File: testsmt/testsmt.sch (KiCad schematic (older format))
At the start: 29 parts

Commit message: schematic nearly done
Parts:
- removed R?: R, symbol Device:R
- added D? (x7): LED, symbol Device:LED
- added R? (x8): 68, symbol Device:R
- R?: value R -> 68
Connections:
- net +3V3: now also U?.10 (~SRCLR), U?.16 (3.3V), U?.16 (VCC), U?.16 (VDD), U?.50 (3.3V)
- net FSR: now also U?.4 (X7)
- net GND: now also D?.1 (K), U?.1 (GND), U?.13 (~OE), U?.17 (GND), U?.39 (GND), U?.8 (GND), D?.1 (K), D?.1 (K), D?.1 (K), D?.1 (K), D?.1 (K), D?.1 (K), D?.1 (K)
- net KNOB_2: now also U?.14 (X1)
- net KNOB_3: now also U?.15 (X2)
- net KNOB_4: now also U?.12 (X3)
- net KNOB_5: now also U?.1 (X4)
- net KNOB_6: now also U?.5 (X5)
- net KNOB_READ: now also U?.3 (X)
- net LDR: now also U?.2 (X6)
- net SHIFT_REG_CLOCK: now also U?.11 (SRCLK)
- net SHIFT_REG_DATA: now also U?.14 (SER)
- net SHIFT_REG_LATCH: now also U?.12 (RCLK)
- net at D?.2 (A): now also R?.1
- net at R?.2: now also U?.1 (QB)
- net at U?.15 (QA): now also R?.2
- net at U?.2 (QC): now also R?.2
- net at U?.3 (QD): now also R?.2
- net at U?.4 (QE): now also R?.2
- net at U?.5 (QF): now also R?.2
- net at U?.6 (QG): now also R?.2
- net at U?.7 (QH): now also R?.2
- new net: D?.2 (A), R?.1 (x7)
- no-connect marks 8 -> 33
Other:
- moved on the sheet: D?, J?, R?, U?

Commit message: schematic looking good
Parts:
- removed U? (x2): 4051, symbol 4xxx:4051
- added C1: C, symbol Device:C
- added C2: 10uF, symbol Device:CP
- added J5: AudioJack3_Ground_Switch, symbol Connector:AudioJack3_Ground_Switch
- added R2: 220, symbol Device:R
- added R3: 470, symbol Device:R
- added RV7: R_POT, symbol Device:R_POT
- gave numbers to parts that had none: 41
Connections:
- net SINGLE_LED is gone; now on an unnamed net: U2.21 (14_A0_SCK)
- net +3V3: now also R3.2; no longer U2.50 (3.3V)
- net DAC_OUTPUT: now also RV7.3
- net GND: now also D1.1 (K), C1.2, J5.S, RV7.1
- net SERIAL_RX: now also U1.6 (VO2), R3.1
- net at D1.2 (A): now also R1.1
- net at J1.4: now also R2.2
- net at J1.5: now also D2.2 (A), U1.3 (C2)
- net +5V: now reaches U2.33 (Vin)
- net +5V: now also U1.8 (VCC), C1.1
- net at U1.2 (C1): now also D2.1 (K), R2.1
- new net: C2.2, J5.R, J5.T
- new net: C2.1, RV7.2
- no-connect marks 33 -> 39
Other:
- moved on the sheet: D1, D2, J1, R1, R4, R5, R6, R7, RV1, RV2, RV3, RV4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

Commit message: nearly done adding footprints
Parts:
- C1: value C -> 0.1uF; footprint (none) -> Capacitor_SMD:C_0805_2012Metric
- C2: footprint (none) -> Capacitor_Tantalum_SMD:CP_EIA-3216-18_Kemet-A
- D1, D10, D3, D4, D5, D6, D7, D8, D9: footprint (none) -> LED_SMD:LED_0805_2012Metric
- D2: footprint Diode_THT:D_DO-35_SOD27_P7.62mm_Horizontal -> Diode_SMD:D_SOD-123
- J2, J3, J4: footprint (none) -> Connector_PinSocket_2.54mm:PinSocket_1x16_P2.54mm_Vertical
- R1, R10, R11, R12, R13, R14, R15, R2, R3, R5, R7, R8, R9: footprint (none) -> Resistor_SMD:R_0805_2012Metric
- R4, R6: footprint (none) -> Connector_PinHeader_2.54mm:PinHeader_1x02_P2.54mm_Vertical
- U1: footprint (none) -> Package_DIP:SMDIP-8_W9.53mm
- U2: footprint (none) -> teensy:Teensy30_31_32_LC
- U3, U4, U5, U6, U7, U8: footprint (none) -> Package_SO:SOIC-16_3.9x9.9mm_P1.27mm
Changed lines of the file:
@@
 F 0 "U4" H 7291 9746 50  0000 L CNN
 F 1 "4051" H 7291 9655 50  0000 L CNN
-F 2 "" H 6750 9700 50  0001 C CNN
+F 2 "Package_SO:SOIC-16_3.9x9.9mm_P1.27mm" H 6750 9700 50  0001 C CNN
 F 3 "http://www.intersil.com/content/dam/Intersil/documents/cd40/cd4051bms-52bms-53bms.pdf" H 6750 9700 50  0001 C CNN
 	1    6750 9700
@@
 F 0 "U7" H 11241 4446 50  0000 L CNN
 F 1 "4051" H 11241 4355 50  0000 L CNN
-F 2 "" H 10700 4400 50  0001 C CNN
+F 2 "Package_SO:SOIC-16_3.9x9.9mm_P1.27mm" H 10700 4400 50  0001 C CNN
 F 3 "http://www.intersil.com/content/dam/Intersil/documents/cd40/cd4051bms-52bms-53bms.pdf" H 10700 4400 50  0001 C CNN
 	1    10700 4400
@@
 F 0 "D1" H 941 7416 50  0000 C CNN
 F 1 "LED" H 941 7325 50  0000 C CNN
-F 2 "" H 950 7200 50  0001 C CNN
+F 2 "LED_SMD:LED_0805_2012Metric" H 950 7200 50  0001 C CNN
 F 3 "~" H 950 7200 50  0001 C CNN
 	1    950  7200
@@
 F 0 "D4" H 13941 1816 50  0000 C CNN
 F 1 "LED" H 13941 1725 50  0000 C CNN
-F 2 "" H 13950 1600 50  0001 C CNN
+F 2 "LED_SMD:LED_0805_2012Metric" H 13950 1600 50  0001 C CNN
 F 3 "~" H 13950 1600 50  0001 C CNN
 	1    13950 1600
@@
 F 0 "R9" H 13720 1646 50  0000 L CNN
 F 1 "68" H 13720 1555 50  0000 L CNN
-F 2 "" V 13580 1600 50  0001 C CNN
+F 2 "Resistor_SMD:R_0805_2012Metric" V 13580 1600 50  0001 C CNN
 F 3 "~" H 13650 1600 50  0001 C CNN
 	1    13650 1600
@@
 F 0 "U2" H 3200 7587 60  0000 C CNN
 F 1 "Teensy3.2" H 3200 7481 60  0000 C CNN
-F 2 "" H 3200 5200 60  0000 C CNN
+F 2 "teensy:Teensy30_31_32_LC" H 3200 5200 60  0001 C CNN
 F 3 "" H 3200 5200 60  0000 C CNN
 	1    3200 6000
@@
 F 0 "J2" H 11880 7092 50  0000 L CNN
 F 1 "Conn_01x16" H 11880 7001 50  0000 L CNN
-F 2 "" H 11800 7100 50  0001 C CNN
+F 2 "Connector_PinSocket_2.54mm:PinSocket_1x16_P2.54mm_Vertical" H 11800 7100 50  0001 C CNN
 F 3 "~" H 11800 7100 50  0001 C CNN
 	1    11800 7100
@@
 F 0 "U1" H 3000 2967 50  0000 C CNN
 F 1 "6N138" H 3000 2876 50  0000 C CNN
-F 2 "" H 3290 2200 50  0001 C CNN
+F 2 "Package_DIP:SMDIP-8_W9.53mm" H 3290 2200 50  0001 C CNN
 F 3 "http://www.onsemi.com/pub/Collateral/HCPL2731-D.pdf" H 3290 2200 50  0001 C CNN
 	1    3000 2500
@@
 F 0 "D2" H 2350 2566 50  0000 C CNN
 F 1 "1N4148" H 2350 2475 50  0000 C CNN
-F 2 "Diode_THT:D_DO-35_SOD27_P7.62mm_Horizontal" H 2350 2175 50  0001 C CNN
+F 2 "Diode_SMD:D_SOD-123" H 2350 2175 50  0001 C CNN
 F 3 "http://www.nxp.com/documents/data_sheet/1N4148_1N4448.pdf" H 2350 2350 50  0001 C CNN
 	1    2350 2350
@@
 F 0 "U3" H 7291 7246 50  0000 L CNN
 F 1 "4051" H 7291 7155 50  0000 L CNN
-F 2 "" H 6750 7200 50  0001 C CNN
+F 2 "Package_SO:SOIC-16_3.9x9.9mm_P1.27mm" H 6750 7200 50  0001 C CNN
 F 3 "http://www.intersil.com/content/dam/Intersil/documents/cd40/cd4051bms-52bms-53bms.pdf" H 6750 7200 50  0001 C CNN
 	1    6750 7200
@@
 F 0 "U8" H 11550 1250 50  0000 C CNN
 F 1 "74HC595" H 11550 1150 50  0000 C CNN
-F 2 "" H 12200 1600 50  0001 C CNN
+F 2 "Package_SO:SOIC-16_3.9x9.9mm_P1.27mm" H 12200 1600 50  0001 C CNN
 F 3 "http://www.ti.com/lit/ds/symlink/sn74hc595.pdf" H 12200 1600 50  0001 C CNN
 	1    12200 1600
@@
 F 0 "U6" H 9991 9746 50  0000 L CNN
 F 1 "4051" H 9991 9655 50  0000 L CNN
-F 2 "" H 9450 9700 50  0001 C CNN
+F 2 "Package_SO:SOIC-16_3.9x9.9mm_P1.27mm" H 9450 9700 50  0001 C CNN
 F 3 "http://www.intersil.com/content/dam/Intersil/documents/cd40/cd4051bms-52bms-53bms.pdf" H 9450 9700 50  0001 C CNN
 	1    9450 9700
@@
 F 0 "U5" H 9991 7246 50  0000 L CNN
 F 1 "4051" H 9991 7155 50  0000 L CNN
-F 2 "" H 9450 7200 50  0001 C CNN
+F 2 "Package_SO:SOIC-16_3.9x9.9mm_P1.27mm" H 9450 7200 50  0001 C CNN
 F 3 "http://www.intersil.com/content/dam/Intersil/documents/cd40/cd4051bms-52bms-53bms.pdf" H 9450 7200 50  0001 C CNN
 	1    9450 7200
@@
 F 0 "J3" H 13180 7092 50  0000 L CNN
 F 1 "Conn_01x16" H 13180 7001 50  0000 L CNN
-F 2 "" H 13100 7100 50  0001 C CNN
+F 2 "Connector_PinSocket_2.54mm:PinSocket_1x16_P2.54mm_Vertical" H 13100 7100 50  0001 C CNN
 F 3 "~" H 13100 7100 50  0001 C CNN
 	1    13100 7100
@@
 F 0 "J4" H 14480 7092 50  0000 L CNN
 F 1 "Conn_01x16" H 14480 7001 50  0000 L CNN
-F 2 "" H 14400 7100 50  0001 C CNN
+F 2 "Connector_PinSocket_2.54mm:PinSocket_1x16_P2.54mm_Vertical" H 14400 7100 50  0001 C CNN
 F 3 "~" H 14400 7100 50  0001 C CNN
 	1    14400 7100
@@
 F 0 "R6" H 6920 4996 50  0000 L CNN
 F 1 "R_FORCE" H 6920 4905 50  0000 L CNN
-F 2 "" V 6900 4700 50  0001 L CNN
+F 2 "Connector_PinHeader_2.54mm:PinHeader_1x02_P2.54mm_Vertical" V 6900 4700 50  0001 L CNN
 F 3 "~" H 6850 4900 50  0001 C CNN
 	1    6850 4950
@@
 F 0 "R4" H 6120 4996 50  0000 L CNN
 F 1 "R_PHOTO" H 6120 4905 50  0000 L CNN
-F 2 "" V 6100 4700 50  0001 L CNN
+F 2 "Connector_PinHeader_2.54mm:PinHeader_1x02_P2.54mm_Vertical" V 6100 4700 50  0001 L CNN
 F 3 "~" H 6050 4900 50  0001 C CNN
 	1    6050 4950
@@
 F 0 "R5" H 6120 5496 50  0000 L CNN
 F 1 "10K" H 6120 5405 50  0000 L CNN
-F 2 "" V 5980 5450 50  0001 C CNN
+F 2 "Resistor_SMD:R_0805_2012Metric" V 5980 5450 50  0001 C CNN
 F 3 "~" H 6050 5450 50  0001 C CNN
 	1    6050 5450
@@
 F 0 "R7" H 6920 5496 50  0000 L CNN
 F 1 "10K" H 6920 5405 50  0000 L CNN
-F 2 "" V 6780 5450 50  0001 C CNN
+F 2 "Resistor_SMD:R_0805_2012Metric" V 6780 5450 50  0001 C CNN
 F 3 "~" H 6850 5450 50  0001 C CNN
 	1    6850 5450
@@
 F 0 "D3" H 13941 1416 50  0000 C CNN
 F 1 "LED" H 13941 1325 50  0000 C CNN
-F 2 "" H 13950 1200 50  0001 C CNN
+F 2 "LED_SMD:LED_0805_2012Metric" H 13950 1200 50  0001 C CNN
 F 3 "~" H 13950 1200 50  0001 C CNN
 	1    13950 1200
@@
 F 0 "R8" H 13720 1246 50  0000 L CNN
 F 1 "68" H 13720 1155 50  0000 L CNN
-F 2 "" V 13580 1200 50  0001 C CNN
+F 2 "Resistor_SMD:R_0805_2012Metric" V 13580 1200 50  0001 C CNN
 F 3 "~" H 13650 1200 50  0001 C CNN
 	1    13650 1200
@@
 F 0 "D6" H 13941 2616 50  0000 C CNN
 F 1 "LED" H 13941 2525 50  0000 C CNN
-F 2 "" H 13950 2400 50  0001 C CNN
+F 2 "LED_SMD:LED_0805_2012Metric" H 13950 2400 50  0001 C CNN
 F 3 "~" H 13950 2400 50  0001 C CNN
 	1    13950 2400
@@
 F 0 "R11" H 13720 2446 50  0000 L CNN
 F 1 "68" H 13720 2355 50  0000 L CNN
-F 2 "" V 13580 2400 50  0001 C CNN
+F 2 "Resistor_SMD:R_0805_2012Metric" V 13580 2400 50  0001 C CNN
 F 3 "~" H 13650 2400 50  0001 C CNN
 	1    13650 2400
@@
 F 0 "D5" H 13941 2216 50  0000 C CNN
 F 1 "LED" H 13941 2125 50  0000 C CNN
-F 2 "" H 13950 2000 50  0001 C CNN
+F 2 "LED_SMD:LED_0805_2012Metric" H 13950 2000 50  0001 C CNN
 F 3 "~" H 13950 2000 50  0001 C CNN
 	1    13950 2000
@@
 F 0 "R10" H 13720 2046 50  0000 L CNN
 F 1 "68" H 13720 1955 50  0000 L CNN
-F 2 "" V 13580 2000 50  0001 C CNN
+F 2 "Resistor_SMD:R_0805_2012Metric" V 13580 2000 50  0001 C CNN
 F 3 "~" H 13650 2000 50  0001 C CNN
 	1    13650 2000
@@
 F 0 "D8" H 13941 3416 50  0000 C CNN
 F 1 "LED" H 13941 3325 50  0000 C CNN
-F 2 "" H 13950 3200 50  0001 C CNN
+F 2 "LED_SMD:LED_0805_2012Metric" H 13950 3200 50  0001 C CNN
 F 3 "~" H 13950 3200 50  0001 C CNN
 	1    13950 3200
@@
 F 0 "R13" H 13720 3246 50  0000 L CNN
 F 1 "68" H 13720 3155 50  0000 L CNN
-F 2 "" V 13580 3200 50  0001 C CNN
+F 2 "Resistor_SMD:R_0805_2012Metric" V 13580 3200 50  0001 C CNN
 F 3 "~" H 13650 3200 50  0001 C CNN
 	1    13650 3200
@@
 F 0 "D7" H 13941 3016 50  0000 C CNN
 F 1 "LED" H 13941 2925 50  0000 C CNN
-F 2 "" H 13950 2800 50  0001 C CNN
+F 2 "LED_SMD:LED_0805_2012Metric" H 13950 2800 50  0001 C CNN
 F 3 "~" H 13950 2800 50  0001 C CNN
 	1    13950 2800
@@
 F 0 "R12" H 13720 2846 50  0000 L CNN
 F 1 "68" H 13720 2755 50  0000 L CNN
-F 2 "" V 13580 2800 50  0001 C CNN
+F 2 "Resistor_SMD:R_0805_2012Metric" V 13580 2800 50  0001 C CNN
 F 3 "~" H 13650 2800 50  0001 C CNN
 	1    13650 2800
@@
 F 0 "D10" H 13941 4216 50  0000 C CNN
 F 1 "LED" H 13941 4125 50  0000 C CNN
-F 2 "" H 13950 4000 50  0001 C CNN
+F 2 "LED_SMD:LED_0805_2012Metric" H 13950 4000 50  0001 C CNN
 F 3 "~" H 13950 4000 50  0001 C CNN
 	1    13950 4000
@@
 F 0 "R15" H 13720 4046 50  0000 L CNN
 F 1 "68" H 13720 3955 50  0000 L CNN
-F 2 "" V 13580 4000 50  0001 C CNN
+F 2 "Resistor_SMD:R_0805_2012Metric" V 13580 4000 50  0001 C CNN
 F 3 "~" H 13650 4000 50  0001 C CNN
 	1    13650 4000
@@
 F 0 "D9" H 13941 3816 50  0000 C CNN
 F 1 "LED" H 13941 3725 50  0000 C CNN
-F 2 "" H 13950 3600 50  0001 C CNN
+F 2 "LED_SMD:LED_0805_2012Metric" H 13950 3600 50  0001 C CNN
 F 3 "~" H 13950 3600 50  0001 C CNN
 	1    13950 3600
@@
 F 0 "R14" H 13720 3646 50  0000 L CNN
 F 1 "68" H 13720 3555 50  0000 L CNN
-F 2 "" V 13580 3600 50  0001 C CNN
+F 2 "Resistor_SMD:R_0805_2012Metric" V 13580 3600 50  0001 C CNN
 F 3 "~" H 13650 3600 50  0001 C CNN
 	1    13650 3600
@@
 F 0 "R1" H 1020 6946 50  0000 L CNN
 F 1 "68" H 1020 6855 50  0000 L CNN
-F 2 "" V 880 6900 50  0001 C CNN
+F 2 "Resistor_SMD:R_0805_2012Metric" V 880 6900 50  0001 C CNN
 F 3 "~" H 950 6900 50  0001 C CNN
 	1    950  6900
@@
 F 0 "R2" V 1843 2000 50  0000 C CNN
 F 1 "220" V 1934 2000 50  0000 C CNN
-F 2 "" V 1980 2000 50  0001 C CNN
+F 2 "Resistor_SMD:R_0805_2012Metric" V 1980 2000 50  0001 C CNN
 F 3 "~" H 2050 2000 50  0001 C CNN
 	1    2050 2000
@@
 F 0 "R3" H 3430 1904 50  0000 R CNN
 F 1 "470" H 3430 1995 50  0000 R CNN
-F 2 "" V 3430 1950 50  0001 C CNN
+F 2 "Resistor_SMD:R_0805_2012Metric" V 3430 1950 50  0001 C CNN
 F 3 "~" H 3500 1950 50  0001 C CNN
 	1    3500 1950
@@
 P 5000 2550
 F 0 "C1" H 5115 2596 50  0000 L CNN
-F 1 "C" H 5115 2505 50  0000 L CNN
-F 2 "" H 5038 2400 50  0001 C CNN
+F 1 "0.1uF" H 5115 2505 50  0000 L CNN
+F 2 "Capacitor_SMD:C_0805_2012Metric" H 5038 2400 50  0001 C CNN
 F 3 "~" H 5000 2550 50  0001 C CNN
 	1    5000 2550
@@
 F 0 "C2" V 7645 2300 50  0000 C CNN
 F 1 "10uF" V 7736 2300 50  0000 C CNN
-F 2 "" H 7938 2150 50  0001 C CNN
+F 2 "Capacitor_Tantalum_SMD:CP_EIA-3216-18_Kemet-A" H 7938 2150 50  0001 C CNN
 F 3 "~" H 7900 2300 50  0001 C CNN
 	1    7900 2300

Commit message: footprints hopefully done
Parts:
- J1: footprint (none) -> polymodsmt:MIDI_DIN5
- J5: footprint (none) -> polymodsmt:Tayda_3.5mm_stereo_TRS_jack_A-853
- RV1, RV2, RV3, RV4, RV5, RV6, RV7: footprint (none) -> Potentiometer_THT:Potentiometer_Alps_RK09K_Single_Vertical
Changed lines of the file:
@@
 F 0 "RV1" H 5980 3796 50  0000 R CNN
 F 1 "R_POT" H 5980 3705 50  0000 R CNN
-F 2 "" H 6050 3750 50  0001 C CNN
+F 2 "Potentiometer_THT:Potentiometer_Alps_RK09K_Single_Vertical" H 6050 3750 50  0001 C CNN
 F 3 "~" H 6050 3750 50  0001 C CNN
 	1    6050 3750
@@
 F 0 "J1" H 1700 2226 50  0000 C CNN
 F 1 "DIN-5_180degree" H 1700 2135 50  0000 C CNN
-F 2 "" H 1700 2500 50  0001 C CNN
+F 2 "polymodsmt:MIDI_DIN5" H 1700 2500 50  0001 C CNN
 F 3 "http://www.mouser.com/ds/2/18/40_c091_abd_e-75918.pdf" H 1700 2500 50  0001 C CNN
 	1    1700 2500
@@
 F 0 "RV3" H 6780 3796 50  0000 R CNN
 F 1 "R_POT" H 6780 3705 50  0000 R CNN
-F 2 "" H 6850 3750 50  0001 C CNN
+F 2 "Potentiometer_THT:Potentiometer_Alps_RK09K_Single_Vertical" H 6850 3750 50  0001 C CNN
 F 3 "~" H 6850 3750 50  0001 C CNN
 	1    6850 3750
@@
 F 0 "RV5" H 7580 3796 50  0000 R CNN
 F 1 "R_POT" H 7580 3705 50  0000 R CNN
-F 2 "" H 7650 3750 50  0001 C CNN
+F 2 "Potentiometer_THT:Potentiometer_Alps_RK09K_Single_Vertical" H 7650 3750 50  0001 C CNN
 F 3 "~" H 7650 3750 50  0001 C CNN
 	1    7650 3750
@@
 F 0 "RV2" H 5980 4396 50  0000 R CNN
 F 1 "R_POT" H 5980 4305 50  0000 R CNN
-F 2 "" H 6050 4350 50  0001 C CNN
+F 2 "Potentiometer_THT:Potentiometer_Alps_RK09K_Single_Vertical" H 6050 4350 50  0001 C CNN
 F 3 "~" H 6050 4350 50  0001 C CNN
 	1    6050 4350
@@
 F 0 "RV4" H 6780 4396 50  0000 R CNN
 F 1 "R_POT" H 6780 4305 50  0000 R CNN
-F 2 "" H 6850 4350 50  0001 C CNN
+F 2 "Potentiometer_THT:Potentiometer_Alps_RK09K_Single_Vertical" H 6850 4350 50  0001 C CNN
 F 3 "~" H 6850 4350 50  0001 C CNN
 	1    6850 4350
@@
 F 0 "RV6" H 7580 4396 50  0000 R CNN
 F 1 "R_POT" H 7580 4305 50  0000 R CNN
-F 2 "" H 7650 4350 50  0001 C CNN
+F 2 "Potentiometer_THT:Potentiometer_Alps_RK09K_Single_Vertical" H 7650 4350 50  0001 C CNN
 F 3 "~" H 7650 4350 50  0001 C CNN
 	1    7650 4350
@@
 F 0 "J5" H 7254 2442 50  0000 C CNN
 F 1 "AudioJack3_Ground_Switch" H 7254 2351 50  0000 C CNN
-F 2 "" H 7250 2100 50  0001 C CNN
+F 2 "polymodsmt:Tayda_3.5mm_stereo_TRS_jack_A-853" H 7250 2100 50  0001 C CNN
 F 3 "~" H 7250 2100 50  0001 C CNN
 	1    7250 2100
@@
 F 0 "RV7" H 8280 2346 50  0000 R CNN
 F 1 "R_POT" H 8280 2255 50  0000 R CNN
-F 2 "" H 8350 2300 50  0001 C CNN
+F 2 "Potentiometer_THT:Potentiometer_Alps_RK09K_Single_Vertical" H 8350 2300 50  0001 C CNN
 F 3 "~" H 8350 2300 50  0001 C CNN
 	1    8350 2300

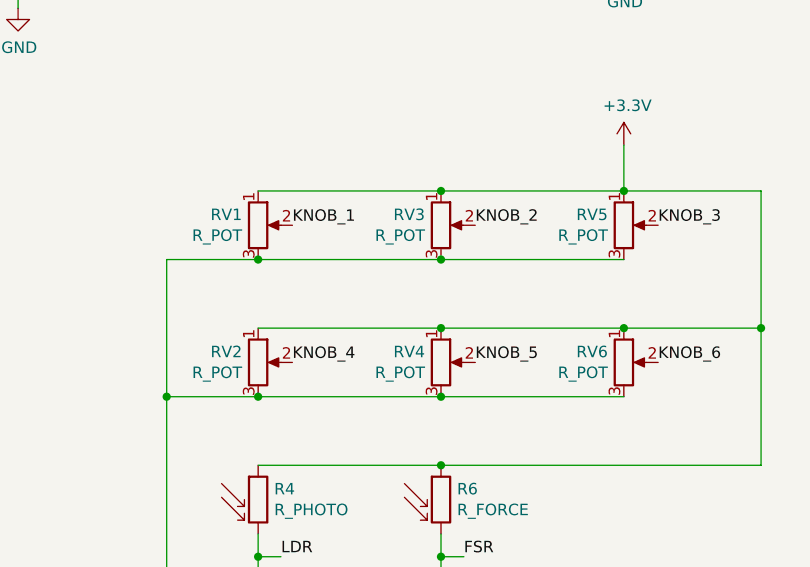
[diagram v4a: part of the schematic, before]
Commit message: started laying out board
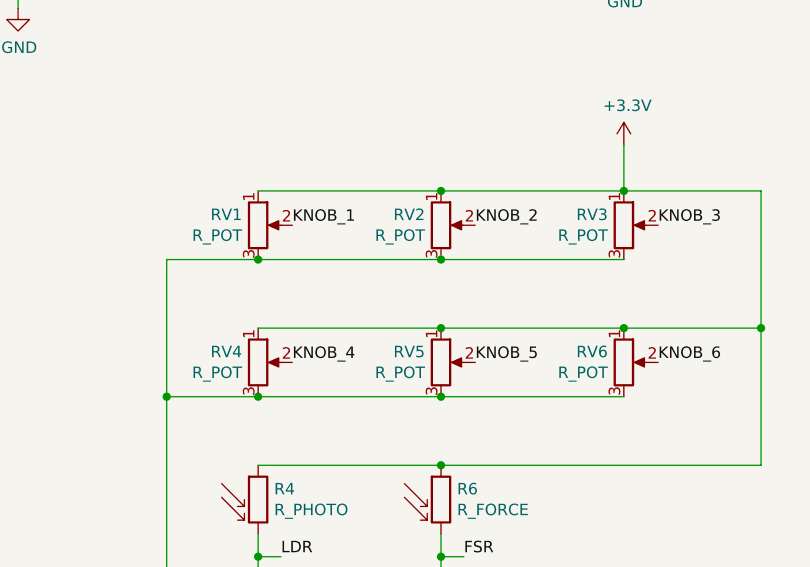
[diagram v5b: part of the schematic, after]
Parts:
- renumbered RV3 to RV2, RV5 to RV3, RV2 to RV4, RV4 to RV5
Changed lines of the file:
@@
 KNOB_1
 $Comp
-L Device:R_POT RV3
+L Device:R_POT RV2
 U 1 1 5E828549
 P 6850 3750
-F 0 "RV3" H 6780 3796 50  0000 R CNN
+F 0 "RV2" H 6780 3796 50  0000 R CNN
 F 1 "R_POT" H 6780 3705 50  0000 R CNN
 F 2 "Potentiometer_THT:Potentiometer_Alps_RK09K_Single_Vertical" H 6850 3750 50  0001 C CNN
@@
 KNOB_2
 $Comp
-L Device:R_POT RV5
+L Device:R_POT RV3
 U 1 1 5E828A25
 P 7650 3750
-F 0 "RV5" H 7580 3796 50  0000 R CNN
+F 0 "RV3" H 7580 3796 50  0000 R CNN
 F 1 "R_POT" H 7580 3705 50  0000 R CNN
 F 2 "Potentiometer_THT:Potentiometer_Alps_RK09K_Single_Vertical" H 7650 3750 50  0001 C CNN
@@
 KNOB_3
 $Comp
-L Device:R_POT RV2
+L Device:R_POT RV4
 U 1 1 5E828A2D
 P 6050 4350
-F 0 "RV2" H 5980 4396 50  0000 R CNN
+F 0 "RV4" H 5980 4396 50  0000 R CNN
 F 1 "R_POT" H 5980 4305 50  0000 R CNN
 F 2 "Potentiometer_THT:Potentiometer_Alps_RK09K_Single_Vertical" H 6050 4350 50  0001 C CNN
@@
 KNOB_4
 $Comp
-L Device:R_POT RV4
+L Device:R_POT RV5
 U 1 1 5E82949C
 P 6850 4350
-F 0 "RV4" H 6780 4396 50  0000 R CNN
+F 0 "RV5" H 6780 4396 50  0000 R CNN
 F 1 "R_POT" H 6780 4305 50  0000 R CNN
 F 2 "Potentiometer_THT:Potentiometer_Alps_RK09K_Single_Vertical" H 6850 4350 50  0001 C CNN

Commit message: mounting holes
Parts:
- added H1, H2, H3, H4: MountingHole, polymodsmt:MountingHole_3.2mm_M3, symbol Mechanical:MountingHole
- RV1, RV2, RV3, RV4, RV5, RV6, RV7: footprint Potentiometer_THT:Potentiometer_Alps_RK09K_Single_Vertical -> polymodsmt:Potentiometer_Alps_RK09K_Single_Vertical
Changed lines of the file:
@@
 F 0 "RV1" H 5980 3796 50  0000 R CNN
 F 1 "R_POT" H 5980 3705 50  0000 R CNN
-F 2 "Potentiometer_THT:Potentiometer_Alps_RK09K_Single_Vertical" H 6050 3750 50  0001 C CNN
+F 2 "polymodsmt:Potentiometer_Alps_RK09K_Single_Vertical" H 6050 3750 50  0001 C CNN
 F 3 "~" H 6050 3750 50  0001 C CNN
 	1    6050 3750
@@
 F 0 "RV2" H 6780 3796 50  0000 R CNN
 F 1 "R_POT" H 6780 3705 50  0000 R CNN
-F 2 "Potentiometer_THT:Potentiometer_Alps_RK09K_Single_Vertical" H 6850 3750 50  0001 C CNN
+F 2 "polymodsmt:Potentiometer_Alps_RK09K_Single_Vertical" H 6850 3750 50  0001 C CNN
 F 3 "~" H 6850 3750 50  0001 C CNN
 	1    6850 3750
@@
 F 0 "RV3" H 7580 3796 50  0000 R CNN
 F 1 "R_POT" H 7580 3705 50  0000 R CNN
-F 2 "Potentiometer_THT:Potentiometer_Alps_RK09K_Single_Vertical" H 7650 3750 50  0001 C CNN
+F 2 "polymodsmt:Potentiometer_Alps_RK09K_Single_Vertical" H 7650 3750 50  0001 C CNN
 F 3 "~" H 7650 3750 50  0001 C CNN
 	1    7650 3750
@@
 F 0 "RV4" H 5980 4396 50  0000 R CNN
 F 1 "R_POT" H 5980 4305 50  0000 R CNN
-F 2 "Potentiometer_THT:Potentiometer_Alps_RK09K_Single_Vertical" H 6050 4350 50  0001 C CNN
+F 2 "polymodsmt:Potentiometer_Alps_RK09K_Single_Vertical" H 6050 4350 50  0001 C CNN
 F 3 "~" H 6050 4350 50  0001 C CNN
 	1    6050 4350
@@
 F 0 "RV5" H 6780 4396 50  0000 R CNN
 F 1 "R_POT" H 6780 4305 50  0000 R CNN
-F 2 "Potentiometer_THT:Potentiometer_Alps_RK09K_Single_Vertical" H 6850 4350 50  0001 C CNN
+F 2 "polymodsmt:Potentiometer_Alps_RK09K_Single_Vertical" H 6850 4350 50  0001 C CNN
 F 3 "~" H 6850 4350 50  0001 C CNN
 	1    6850 4350
@@
 F 0 "RV6" H 7580 4396 50  0000 R CNN
 F 1 "R_POT" H 7580 4305 50  0000 R CNN
-F 2 "Potentiometer_THT:Potentiometer_Alps_RK09K_Single_Vertical" H 7650 4350 50  0001 C CNN
+F 2 "polymodsmt:Potentiometer_Alps_RK09K_Single_Vertical" H 7650 4350 50  0001 C CNN
 F 3 "~" H 7650 4350 50  0001 C CNN
 	1    7650 4350
@@
 F 0 "RV7" H 8280 2346 50  0000 R CNN
 F 1 "R_POT" H 8280 2255 50  0000 R CNN
-F 2 "Potentiometer_THT:Potentiometer_Alps_RK09K_Single_Vertical" H 8350 2300 50  0001 C CNN
+F 2 "polymodsmt:Potentiometer_Alps_RK09K_Single_Vertical" H 8350 2300 50  0001 C CNN
 F 3 "~" H 8350 2300 50  0001 C CNN
 	1    8350 2300
@@
 	7550 2300 7750 2300
 Connection ~ 7550 2300
+$Comp
+L Mechanical:MountingHole H1
+U 1 1 5E851B11
+P 1750 9100
+F 0 "H1" H 1850 9146 50  0000 L CNN
+F 1 "MountingHole" H 1850 9055 50  0000 L CNN
+F 2 "polymodsmt:MountingHole_3.2mm_M3" H 1750 9100 50  0001 C CNN
+F 3 "~" H 1750 9100 50  0001 C CNN
+	1    1750 9100
+	1    0    0    -1
+$EndComp
+$Comp
+L Mechanical:MountingHole H2
+U 1 1 5E851CE3
+P 1750 9350
+F 0 "H2" H 1850 9396 50  0000 L CNN
+F 1 "MountingHole" H 1850 9305 50  0000 L CNN
+F 2 "polymodsmt:MountingHole_3.2mm_M3" H 1750 9350 50  0001 C CNN
+F 3 "~" H 1750 9350 50  0001 C CNN
+	1    1750 9350
+	1    0    0    -1
+$EndComp
+$Comp
+L Mechanical:MountingHole H3
+U 1 1 5E851D5F
+P 1750 9600
+F 0 "H3" H 1850 9646 50  0000 L CNN
+F 1 "MountingHole" H 1850 9555 50  0000 L CNN
+F 2 "polymodsmt:MountingHole_3.2mm_M3" H 1750 9600 50  0001 C CNN
+F 3 "~" H 1750 9600 50  0001 C CNN
+	1    1750 9600
+	1    0    0    -1
+$EndComp
+$Comp
+L Mechanical:MountingHole H4
+U 1 1 5E851DDB
+P 1750 9850
+F 0 "H4" H 1850 9896 50  0000 L CNN
+F 1 "MountingHole" H 1850 9805 50  0000 L CNN
+F 2 "polymodsmt:MountingHole_3.2mm_M3" H 1750 9850 50  0001 C CNN
+F 3 "~" H 1750 9850 50  0001 C CNN
+	1    1750 9850
+	1    0    0    -1
+$EndComp
 $EndSCHEMATC
